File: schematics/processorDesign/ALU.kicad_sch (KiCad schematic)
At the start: 17 parts

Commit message: the interrupt is now working correctly
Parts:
- added U? (x2): 4081, symbol 4xxx:4081
- added U? (x4): 74HC86, symbol 74xx:74HC86
- added U?: MUX_12x1, symbol computerArchProj:MUX_12x1
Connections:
- net at U?. (Z): now also U?. (select) (x6)
- net at U. (Z): now also U?. (select); no longer U?. (select) (x2)
- net at U?. (Z): now also U?. (select); no longer U?. (select) (x2)
- new net: U?. (Z), U?. (select) (x11)
- new net: U?.1, U?.6 (x2)
- new net: U?.2, U?.6 (x2)
- new net: U?. (select), U?.3 (x2)
- new net: U?.4, U?.5 (x2)
- new net: U?.5, U?.5
- new net: U?. (Z), U?. (select), U?. (select)
- new net: U. (Z), U?. (select) (x4)
- new net: U?.4, U?.4
- new net OVF_in: U?. (select)
- new net OVF_out: U?. (select)
- now unconnected: U?. (select)
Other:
- note added: "RES[15]"
- note added: "RES[31]"
- note added: "Rdst[15]"
- note added: "Rsrc[15]"

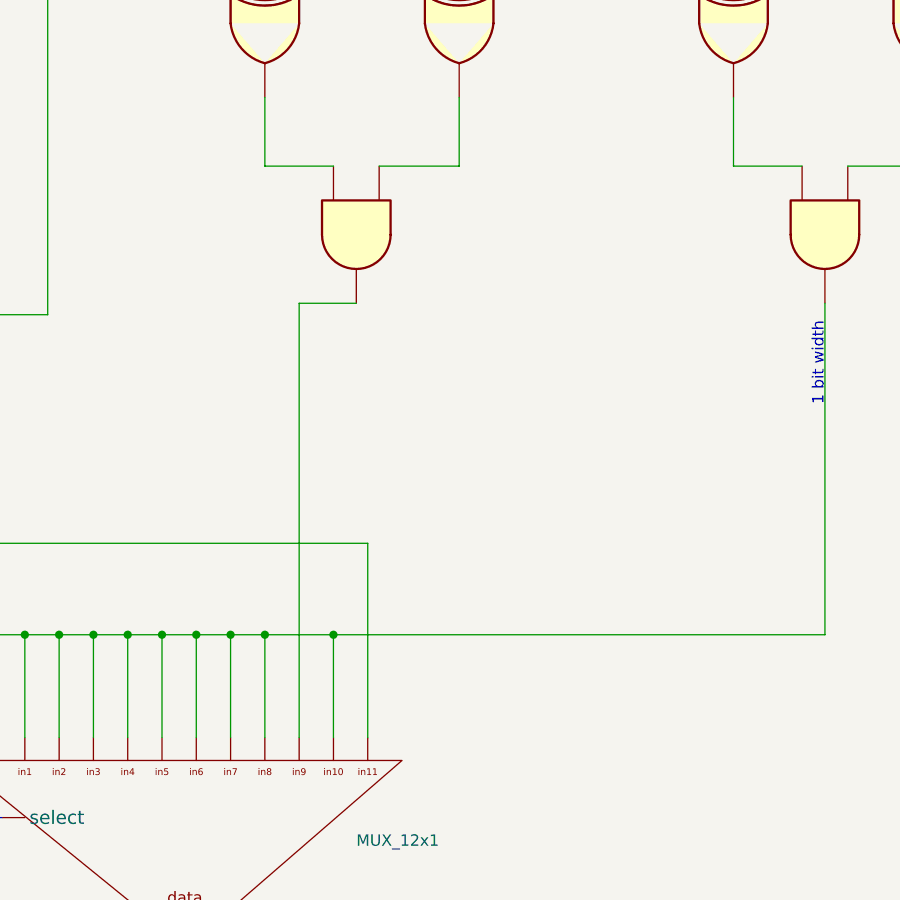
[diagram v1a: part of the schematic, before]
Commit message: the processor is up and running tested and verified, need only tests for some bonus instructions like all I_types instruction except LDM , MUL , DIV , testing EDU and HDU
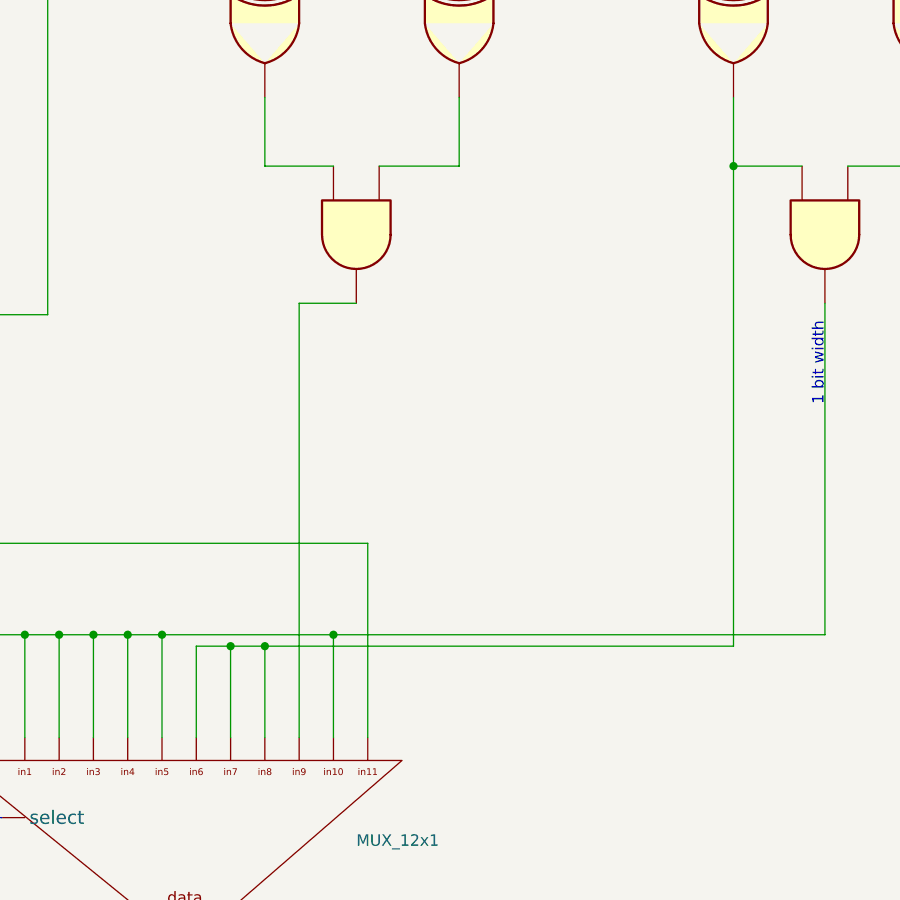
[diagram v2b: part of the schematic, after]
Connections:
- net at U?. (Z): now also U?. (select) (x6)
- net at U. (Z): now also U?. (select); no longer U?. (select) (x2)
- net at U?. (Z): now also U?. (select); no longer U?. (select) (x2)
- net at U?.2, U?.6: now also U?. (select)
- new net: U?. (Z), U?. (select) (x11)
- new net: U?. (Z), U?. (select), U?. (select)
- new net: U. (Z), U?. (select) (x4)
- now unconnected: U?. (select)
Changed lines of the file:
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@@
   (junction (at 521.97 132.08) (diameter 0) (color 0 0 0 0)
   )
+  (junction (at 447.04 232.41) (diameter 0) (color 0 0 0 0)
+  )
   (junction (at 36.83 60.96) (diameter 0) (color 0 0 0 0)
   )
@@
   (junction (at 149.86 171.45) (diameter 0) (color 0 0 0 0)
   )
-  (junction (at 443.23 231.14) (diameter 0) (color 0 0 0 0)
-  )
   (junction (at 179.07 184.15) (diameter 0) (color 0 0 0 0)
   )
-  (junction (at 447.04 231.14) (diameter 0) (color 0 0 0 0)
-  )
   (junction (at 50.8 229.87) (diameter 0) (color 0 0 0 0)
   )
+  (junction (at 450.85 232.41) (diameter 0) (color 0 0 0 0)
+  )
   (junction (at 435.61 231.14) (diameter 0) (color 0 0 0 0)
   )
@@
   (junction (at 46.99 229.87) (diameter 0) (color 0 0 0 0)
   )
-  (junction (at 450.85 231.14) (diameter 0) (color 0 0 0 0)
-  )
   (junction (at 36.83 46.99) (diameter 0) (color 0 0 0 0)
   )
@@
   )
   (junction (at 69.85 229.87) (diameter 0) (color 0 0 0 0)
+  )
+  (junction (at 502.92 179.07) (diameter 0) (color 0 0 0 0)
   )
   (no_connect (at 113.03 55.88))
@@
     (stroke (width 0) (type default) (color 0 0 0 0))
   )
+  (wire (pts (xy 450.85 232.41) (xy 447.04 232.41))
+    (stroke (width 0) (type default) (color 207 94 255 1))
+  )
   (bus (pts (xy 184.15 134.62) (xy 184.15 162.56))
     (stroke (width 0) (type default) (color 0 0 0 0))
@@
     (stroke (width 0) (type default) (color 247 53 255 1))
   )
-  (wire (pts (xy 443.23 231.14) (xy 443.23 242.57))
-    (stroke (width 0) (type default) (color 0 0 0 0))
-  )
   (bus (pts (xy 93.98 250.19) (xy 100.33 250.19))
     (stroke (width 0) (type default) (color 0 0 0 0))
+  )
+  (wire (pts (xy 450.85 232.41) (xy 450.85 242.57))
+    (stroke (width 0) (type default) (color 207 94 255 1))
   )
   (wire (pts (xy 335.28 181.61) (xy 335.28 195.58))
@@
     (stroke (width 0) (type default) (color 0 0 0 0))
   )
-  (wire (pts (xy 443.23 231.14) (xy 447.04 231.14))
-    (stroke (width 0) (type default) (color 0 0 0 0))
-  )
   (wire (pts (xy 403.86 25.4) (xy 403.86 220.98))
     (stroke (width 0) (type default) (color 80 199 205 1))
@@
     (stroke (width 0) (type default) (color 0 0 0 0))
   )
+  (wire (pts (xy 447.04 232.41) (xy 447.04 242.57))
+    (stroke (width 0) (type default) (color 207 94 255 1))
+  )
   (bus (pts (xy 389.89 287.02) (xy 389.89 251.46))
     (stroke (width 0) (type default) (color 0 0 0 0))
@@
     (stroke (width 0) (type default) (color 0 0 0 0))
   )
+  (wire (pts (xy 447.04 232.41) (xy 443.23 232.41))
+    (stroke (width 0) (type default) (color 207 94 255 1))
+  )
   (wire (pts (xy 152.4 142.24) (xy 152.4 213.36))
     (stroke (width 0) (type default) (color 0 0 0 0))
@@
     (stroke (width 0) (type default) (color 0 0 0 0))
   )
-  (wire (pts (xy 439.42 231.14) (xy 443.23 231.14))
+  (wire (pts (xy 439.42 231.14) (xy 458.47 231.14))
     (stroke (width 0) (type default) (color 0 0 0 0))
   )
   (bus (pts (xy 332.74 139.7) (xy 292.1 139.7))
     (stroke (width 0) (type default) (color 0 0 0 0))
+  )
+  (wire (pts (xy 502.92 232.41) (xy 450.85 232.41))
+    (stroke (width 0) (type default) (color 207 94 255 1))
   )
   (bus (pts (xy 116.84 129.54) (xy 116.84 146.05))
@@
   )
   (wire (pts (xy 502.92 179.07) (xy 502.92 171.45))
-    (stroke (width 0) (type default) (color 0 0 0 0))
+    (stroke (width 0) (type default) (color 207 94 255 1))
   )
   (bus (pts (xy 149.86 171.45) (xy 158.75 171.45))
@@
     (stroke (width 0) (type default) (color 247 53 255 1))
   )
-  (wire (pts (xy 450.85 231.14) (xy 458.47 231.14))
-    (stroke (width 0) (type default) (color 0 0 0 0))
-  )
   (wire (pts (xy 243.84 262.89) (xy 243.84 271.78))
     (stroke (width 0) (type default) (color 0 0 0 0))
@@
     (stroke (width 0) (type default) (color 0 0 0 0))
   )
-  (wire (pts (xy 447.04 231.14) (xy 450.85 231.14))
-    (stroke (width 0) (type default) (color 0 0 0 0))
-  )
   (wire (pts (xy 69.85 132.08) (xy 31.75 132.08))
     (stroke (width 0) (type default) (color 53 179 202 1))
@@
   )
   (wire (pts (xy 510.54 179.07) (xy 502.92 179.07))
-    (stroke (width 0) (type default) (color 0 0 0 0))
+    (stroke (width 0) (type default) (color 207 94 255 1))
   )
   (bus (pts (xy 59.69 151.13) (xy 157.48 151.13))
@@
     (stroke (width 0) (type default) (color 0 0 0 0))
   )
+  (wire (pts (xy 502.92 179.07) (xy 502.92 232.41))
+    (stroke (width 0) (type default) (color 207 94 255 1))
+  )
   (wire (pts (xy 156.21 121.92) (xy 156.21 128.27))
     (stroke (width 0) (type default) (color 247 53 255 1))
@@
   )
   (bus (pts (xy 86.36 101.6) (xy 166.37 101.6))
-    (stroke (width 0) (type default) (color 0 0 0 0))
-  )
-  (wire (pts (xy 447.04 231.14) (xy 447.04 242.57))
     (stroke (width 0) (type default) (color 0 0 0 0))
   )
@@
     (stroke (width 0) (type default) (color 247 53 255 1))
   )
-  (wire (pts (xy 450.85 231.14) (xy 450.85 242.57))
-    (stroke (width 0) (type default) (color 0 0 0 0))
-  )
   (wire (pts (xy 448.31 148.59) (xy 448.31 156.21))
     (stroke (width 0) (type default) (color 255 119 145 1))
@@
     (stroke (width 0) (type default) (color 0 0 0 0))
   )
+  (wire (pts (xy 443.23 232.41) (xy 443.23 242.57))
+    (stroke (width 0) (type default) (color 207 94 255 1))
+  )
   (wire (pts (xy 142.24 223.52) (xy 222.25 223.52))

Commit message: the processor is now up and running , tested and verified , except for the part related to labels due to a bug in the assembler
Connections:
- net at U?. (Z): now also U?. (select) (x6)
- net at U. (Z): now also U?. (select); no longer U?. (select) (x2)
- net at U?. (Z): now also U?. (select); no longer U?. (select) (x2)
- new net: U?. (Z), U?. (select) (x11)
- new net: U?. (Z), U?. (select), U?. (select)
- new net: U. (Z), U?. (select) (x4)
- now unconnected: U?. (select)

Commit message: the processor is now up and running , tested and verified completly for almost most of the things
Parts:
- added U?: MOD, symbol computerArchProj:MOD
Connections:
- net at U?. (Z): now also U?. (select) (x6)
- net at U. (Z): now also U?. (select); no longer U?. (select) (x2)
- net at U?. (Z): now also U?. (select); no longer U?. (select) (x2)
- new net: U?. (Z), U?. (select) (x13)
- new net: U. (Z), U?. (select) (x4)
- now unconnected: U?. (select)
- no-connect marks 4 -> 10

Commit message: added small code to EDU
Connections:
- net at U?. (Z): now also U?. (select) (x6)
- net at U?. (Z): now also U?. (select); no longer U?. (select) (x3)
- net at U. (Z): now also U?. (select); no longer U?. (select) (x2)
- new net: U?. (Z), U?. (select) (x12)
- new net: U. (Z), U?. (select) (x4)
